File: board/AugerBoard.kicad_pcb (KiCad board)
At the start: 2 copper layers, 257.9 x 95.6 mm, 163 parts, among them J1 RJ45_LED_Shielded, J3 2002411212, J4 2002411212, J5 2002411212, J6 2002411212, J7 2002411212, Q1 BSS138, Q2 BSS138, Q3 BSS138, Q4 BSS138, Q5 BSS138, Q6 BSS138, Q7 BSS138, Q8 BSS138, Q9 BSS138, SW1 SW_Push, SW10 SW_SPDT, SW2 SW_Push, SW3 SW_Push, SW4 SW_Push, SW5 SW_Push, SW6 SW_Push, SW7 SW_Push, SW8 SW_Push, SW9 SW_Push, U1 OKI 5V, U2 Teensy4.1_DEV-16771, U3 ATA6561, U4 OKI 3V3, U5 ATA6561

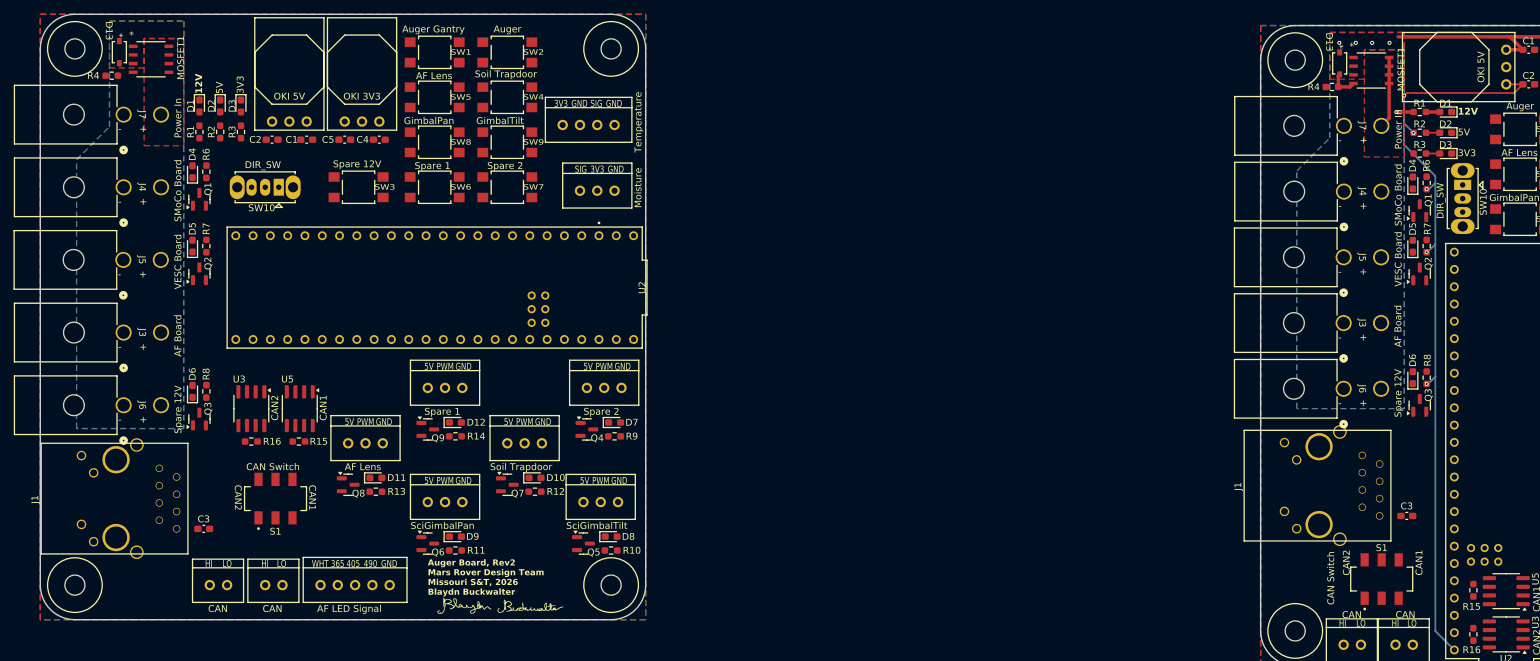
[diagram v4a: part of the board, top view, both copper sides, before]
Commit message: updated teensy pinout
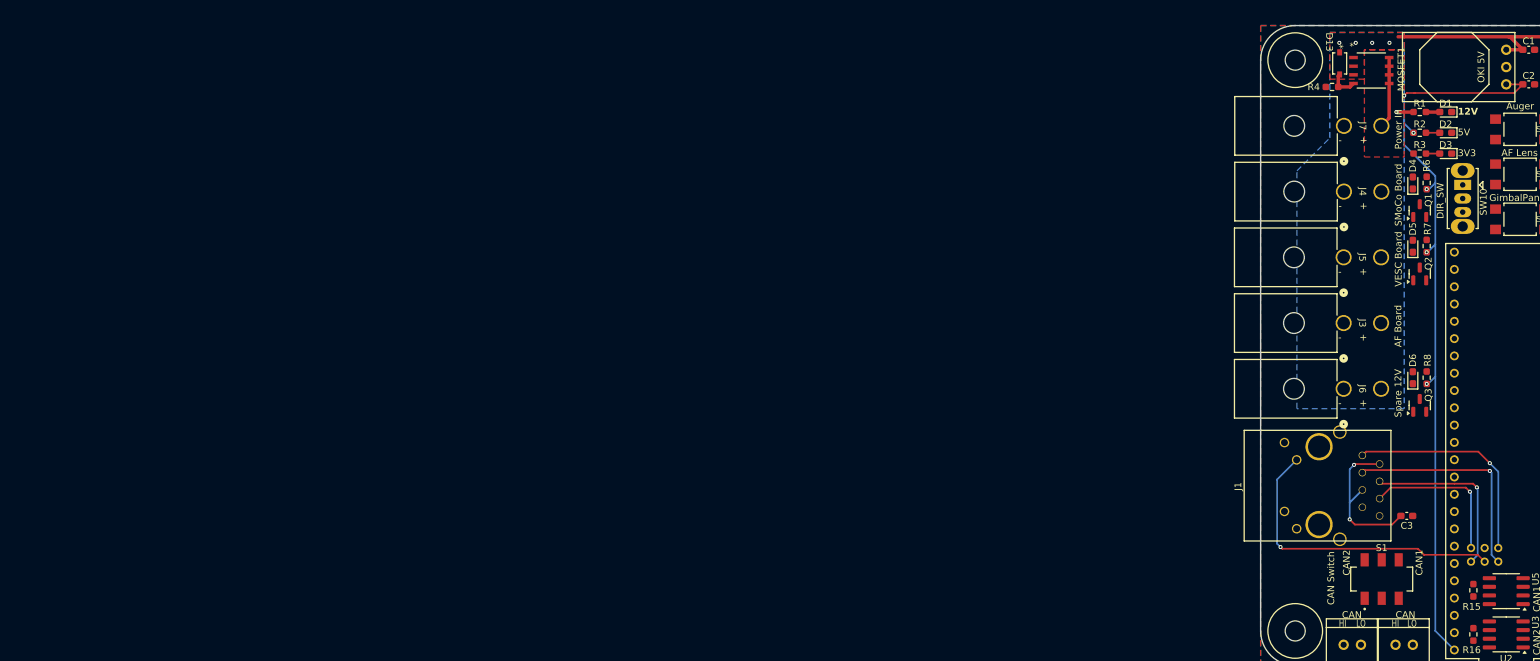
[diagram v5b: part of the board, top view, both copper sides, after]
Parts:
- removed the C1 at (-76.6, 82.8)
- removed the C2 at (-81.7, 82.8)
- removed the C3 at (-91.7, 140.0)
- removed the C4 at (-65.9, 82.8)
- removed the C5 at (-71.0, 82.8)
- removed the Conn1 at (-74.5, 148.2)
- removed the Conn10 at (-58.8, 119.3)
- removed the Conn12 at (-90.8, 148.2)
- removed the Conn13 at (-82.7, 148.2)
- removed the Conn2 at (-47.1, 127.4)
- removed the Conn3 at (-70.5, 127.4)
- removed the Conn4 at (-58.8, 136.0)
- removed the Conn5 at (-35.4, 119.3)
- removed the Conn6 at (-35.9, 136.0)
- removed the Conn7 at (-39.0, 80.6)
- removed the Conn9 at (-36.4, 90.3)
- removed the D1 at (-92.3, 77.9)
- removed the D10 at (-43.1, 132.5)
- removed the D11 at (-66.4, 132.5)
- removed the D12 at (-54.7, 124.3)
- removed the D13 at (-104.1, 70.0)
- removed the D2 at (-89.3, 77.9)
- removed the D3 at (-86.2, 77.9)
- removed the D4 at (-93.3, 87.5)
- removed the D5 at (-93.3, 98.4)
- removed the D6 at (-93.3, 119.8)
- removed the D7 at (-31.4, 124.3)
- removed the D8 at (-31.9, 141.1)
- removed the D9 at (-54.7, 141.1)
- removed the G*** at (-47.1, 151.6)
- removed the H1 at (-35.9, 144.2)
- removed the H2 at (-106.6, 144.2)
- removed the H3 at (-106.6, 73.5)
- removed the H4 at (-35.9, 73.5)
- removed the J1 at (-117.6, 135.6)
- removed the J3 at (-103.5, 111.1)
- removed the J4 at (-103.5, 89.8)
- removed the J5 at (-103.5, 100.5)
- removed the J6 at (-103.5, 121.8)
- removed the J7 at (-103.5, 79.1)
- removed the MOSFET1 at (-99.4, 71.0)
- removed the Q1 at (-92.3, 91.6)
- removed the Q2 at (-92.3, 102.5)
- removed the Q3 at (-92.3, 123.8)
- removed the Q4 at (-35.4, 125.3)
- removed the Q5 at (-35.9, 142.1)
- removed the Q6 at (-58.8, 142.1)
- removed the Q7 at (-47.1, 133.5)
- removed the Q8 at (-70.5, 133.5)
- removed the Q9 at (-58.8, 125.3)
- removed the R1 at (-92.3, 81.7)
- removed the R10 at (-31.9, 143.1)
- removed the R11 at (-54.7, 143.1)
- removed the R12 at (-43.1, 134.5)
- removed the R13 at (-66.4, 134.5)
- removed the R14 at (-54.7, 126.4)
- removed the R15 at (-77.7, 127.1)
- removed the R16 at (-84.7, 127.1)
- removed the R2 at (-89.3, 81.7)
- removed the R3 at (-86.2, 81.7)
- removed the R4 at (-105.2, 73.4)
- removed the R6 at (-91.3, 87.5)
- removed the R7 at (-91.3, 98.4)
- removed the R8 at (-91.3, 119.8)
- removed the R9 at (-31.4, 126.4)
- removed the S1 at (-81.2, 135.5)
- removed the SW1 at (-57.8, 70.0)
- removed the SW10 at (-80.7, 89.8)
- removed the SW2 at (-47.1, 70.0)
- removed the SW3 at (-69.0, 89.8)
- removed the SW4 at (-47.1, 76.6)
- removed the SW5 at (-57.8, 76.6)
- removed the SW6 at (-57.8, 89.8)
- removed the SW7 at (-47.1, 89.8)
- removed the SW8 at (-57.8, 83.2)
- removed the SW9 at (-47.1, 83.2)
- removed the U1 at (-76.6, 80.1)
- removed the U2 at (-57.8, 104.5)
- removed the U3 at (-84.7, 122.3)
- removed the U4 at (-65.9, 80.1)
- removed the U5 at (-77.6, 122.3)
- turned C3 to 180 degrees
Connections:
- U2 pad 10: /Teensy/GimbalPanSW -> /Power/GimbalTiltLED
- U2 pad 11: /Teensy/AFLensSW -> /Servos/SciGimbalTilt
- U2 pad 12: /Teensy/GantrySW -> /Servos/SciGimbalPan
- U2 pad 13: /Servos/SciGimbalPan -> /Power/Spare12VLED
- U2 pad 14: /Servos/SparePWM1 -> /Teensy/SoilDoorSW
- U2 pad 15: /Servos/SoilTrapdoorPWM -> /Teensy/GimbalTiltSW
- U2 pad 16: /Power/SpareLED1 -> /Teensy/SpareSW_12V
- U2 pad 17: /Power/SoilTDLED -> /Teensy/SpareSW1
- U2 pad 18: /Servos/SparePWM2 -> /Teensy/SpareSW2
- U2 pad 19: /Servos/SciGimbalTilt -> unconnected-(U2-A5-Pad19)
- U2 pad 2: unconnected-(U2-OUT2-Pad2) -> /Communications/STBY2
- U2 pad 20: /Power/GimbalTiltLED -> unconnected-(U2-A6-Pad20)
- U2 pad 21: /Power/SpareLED2 -> unconnected-(U2-A7-Pad21)
- U2 pad 24: /Soil Sensors/Moisture -> /AF interface/AFWhiteLED
- U2 pad 25: /Soil Sensors/Temp -> /AF interface/AFLED365
- U2 pad 26: /Teensy/SpareSW_12V -> /AF interface/AFLED405
- U2 pad 27: /Communications/STBY1 -> /AF interface/AFLED490
- U2 pad 28: /Communications/STBY2 -> /Servos/AFLensPWM
- U2 pad 29: /Teensy/Dir_Switch -> /Servos/SoilTrapdoorPWM
- U2 pad 30: /Power/GantryLED -> /Power/SoilTDLED
- U2 pad 31: unconnected-(U2-CTX3-Pad31) -> /Power/AFFLED
- U2 pad 33: /Power/Spare12VLED -> /Power/GantryLED
- U2 pad 35: /Power/AFFLED -> /Teensy/Dir_Switch
- U2 pad 36: /Power/GimbalPanLED -> /Teensy/AugerSW
- U2 pad 37: /Servos/AFLensPWM -> /Teensy/AFLensSW
- U2 pad 38: /AF interface/AFWhiteLED -> /Soil Sensors/Temp
- U2 pad 39: /AF interface/AFLED365 -> /Soil Sensors/Moisture
- U2 pad 4: unconnected-(U2-BCLK2-Pad4) -> /Communications/STBY1
- U2 pad 40: /AF interface/AFLED405 -> /Teensy/GimbalPanSW
- U2 pad 41: /AF interface/AFLED490 -> /Teensy/GantrySW
- U2 pad 5: /Teensy/SpareSW2 -> /Power/GimbalPanLED
- U2 pad 6: /Teensy/GimbalTiltSW -> /Power/SpareLED2
- U2 pad 7: /Teensy/SoilDoorSW -> /Power/SpareLED1
- U2 pad 8: /Teensy/AugerSW -> /Servos/SparePWM2
- U2 pad 9: /Teensy/SpareSW1 -> /Servos/SparePWM1
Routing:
- net /Communications/LED: track 0.00 -> 45.1 mm, vias 0 -> 1
- net /Communications/T+: track 0.00 -> 32.8 mm, vias 0 -> 1
- net /Communications/T-: track 0.00 -> 32.8 mm, vias 0 -> 1
- net /Communications/R+: track 0.00 -> 26.0 mm, vias 0 -> 1
- net Net-(C3-Pad2): track 0.00 -> 23.1 mm, vias 0 -> 2
- net /Communications/R-: track 0.00 -> 22.5 mm, vias 0 -> 1
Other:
- board size 257.9 x 95.6 mm -> 78.7 x 94 mm

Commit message: trace progress
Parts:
- moved Conn12 0.64 mm to (76.3, 157.0)
- moved Conn13 0.64 mm to (83.9, 157.0)
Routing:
- net +3.3V: track 2.44 -> 136.1 mm, vias 0 -> 4
- net +5V: track 112.6 -> 143.9 mm, vias 5 -> 9
- net Net-(U3-CANH): track 0.00 -> 23.3 mm, vias 0 -> 2
- net Net-(U3-CANL): track 0.00 -> 21.4 mm
- net /Communications/STBY2: track 0.00 -> 16.2 mm, vias 0 -> 1
- net Net-(U5-CANH): track 0.00 -> 15.9 mm
- net Net-(U5-CANL): track 0.00 -> 14.8 mm, vias 0 -> 2
- net /Communications/STBY1: track 0.00 -> 14.5 mm, vias 0 -> 1
- net /Communications/TXD1: track 0.00 -> 11.5 mm, vias 0 -> 1
- net /Communications/RXD1: track 0.00 -> 11.3 mm, vias 0 -> 1
- net /Communications/TXD2: track 0.00 -> 7.97 mm, vias 0 -> 1
- net /Communications/RXD2: track 0.00 -> 5.83 mm
- net /Communications/R-: track 22.5 -> 25.9 mm
- net /Communications/T+: track 32.8 -> 34.4 mm

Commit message: preliminary routing
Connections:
- U2 pad 38: /Soil Sensors/Temp -> /Soil Sensors/Moisture
- U2 pad 39: /Soil Sensors/Moisture -> /Soil Sensors/Temp
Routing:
- net +5V: track 143.9 -> 335.2 mm, vias 9 -> 13
- net /Soil Sensors/Temp: track 0.00 -> 78.5 mm, vias 0 -> 1
- net /Teensy/SpareSW_12V: track 0.00 -> 70.9 mm, vias 0 -> 1
- net /Teensy/SpareSW2: track 0.00 -> 67.2 mm, vias 0 -> 2
- net /Soil Sensors/Moisture: track 0.00 -> 67.2 mm, vias 0 -> 1
- net /Teensy/SpareSW1: track 0.00 -> 67.1 mm, vias 0 -> 1
- net /Teensy/GantrySW: track 0.00 -> 54.2 mm, vias 0 -> 1
- net /Teensy/GimbalTiltSW: track 0.00 -> 54.0 mm, vias 0 -> 1
- net /Teensy/SoilDoorSW: track 0.00 -> 47.4 mm, vias 0 -> 1
- net /AF interface/AFLED490: track 0.00 -> 43.0 mm
- net /AF interface/AFLED405: track 0.00 -> 39.5 mm
- net /Teensy/AugerSW: track 0.00 -> 36.9 mm, vias 0 -> 1
- net /AF interface/AFLED365: track 0.00 -> 35.6 mm
- net Net-(Conn12-Pad2): track 0.00 -> 34.6 mm
- net /Teensy/GimbalPanSW: track 0.00 -> 33.8 mm, vias 0 -> 1
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
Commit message: Pre-board check layout
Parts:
- added G***: LOGO, MRDT_Silkscreens:0_MRDT_Logo_10mm, F.Cu at (130.4, 72.0)
- moved G*** 108.9 mm to (102.7, 112.5)
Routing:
- net /Power/GimbalPanLED: track 0.00 -> 25.0 mm
- net /Teensy/SoilDoorSW: track 47.4 -> 54.6 mm
- net GND: vias 0 -> 383
- net +12V: vias 5 -> 3
